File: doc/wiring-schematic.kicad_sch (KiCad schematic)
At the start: 4 parts

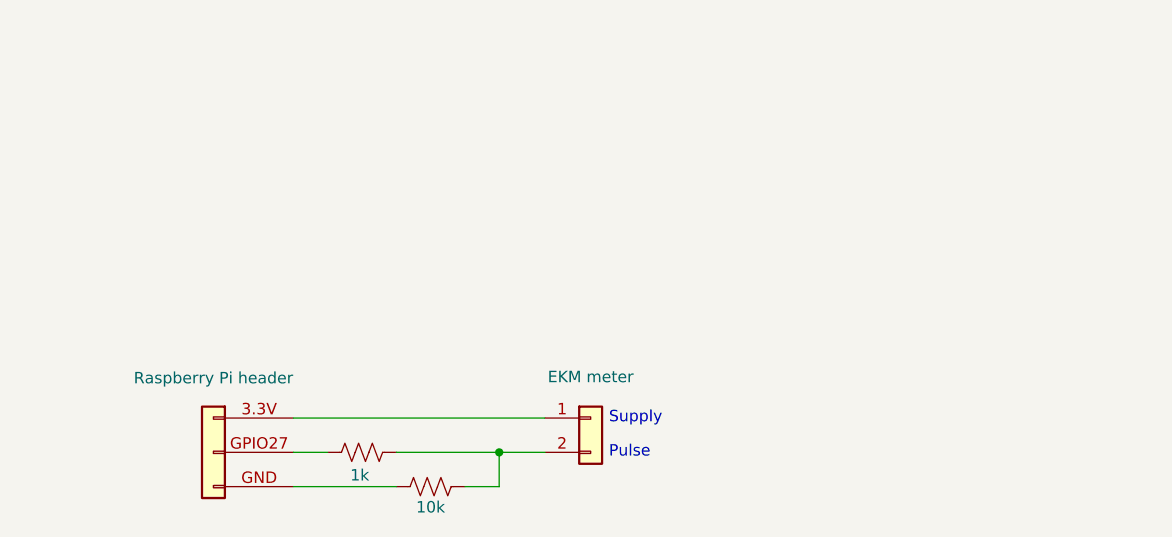
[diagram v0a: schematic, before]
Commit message: Rewire meter input as pull-up, add isolated option
The old wiring ran the bare 3.3 V rail out to the meter. Now the cable
only sees 3.3 V through a 1k pull-up. Also document an optocoupler-
isolated circuit for long runs or where surges are a concern.
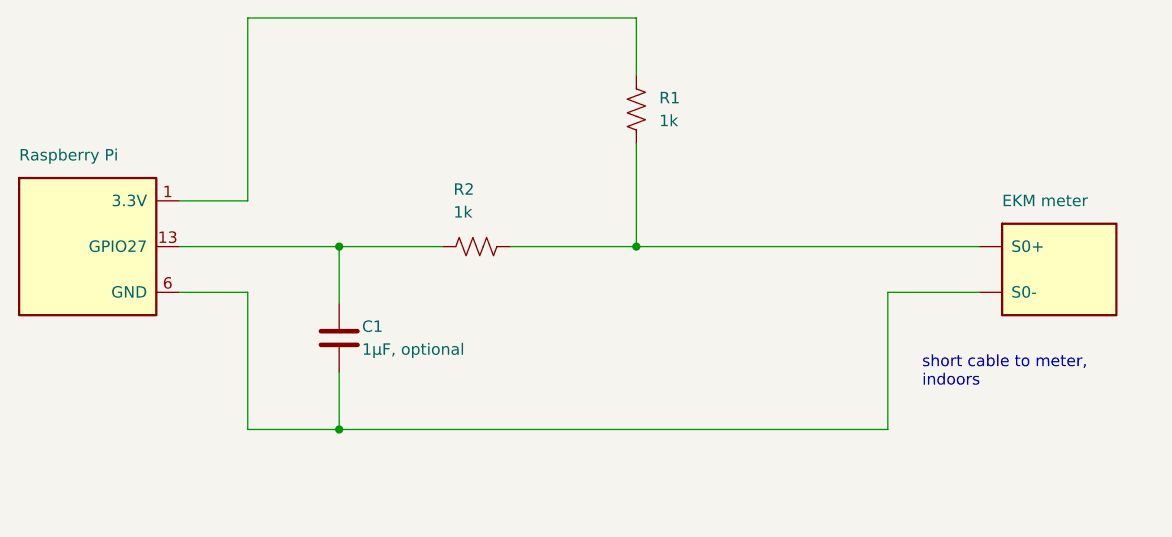
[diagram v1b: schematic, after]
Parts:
- removed J?: EKM meter, symbol Connector_Generic:Conn_01x02
- removed R?: 10k, symbol Device:R_US
- removed U?: Raspberry Pi header, symbol Connector_Generic:Conn_01x03
- added C1: 1µF, optional, symbol Device:C
- added J1: Raspberry Pi, symbol ekm:Raspberry Pi
- added J2: EKM meter, symbol ekm:EKM meter
- added R2: 1k, symbol Device:R_US
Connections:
- net at R1.2: now also J2.1 (S0+), R2.2
- net at R1.1: now also J1.1 (3.3V)
- new net: C1.2, J1.6 (GND), J2.2 (S0-)
- new net: C1.1, J1.13 (GPIO27), R2.1
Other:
- note added: "short cable to meter, indoors"
- note removed: "Pulse"
- note removed: "Supply"
- title: EKM Meter Wiring -> EKM meter wiring: simple
